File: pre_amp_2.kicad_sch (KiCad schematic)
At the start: 55 parts, among them J1 IN, J10 SW2_3, J11 SW2_1, J12 SW2_4, J13 VR5_3, J14 VR5_1, J15 OUT, J2 GND2, J3 Vin, J4 GND, J5 VR1_1, J6 VR3_3, J7 VR1_3, J9 VR4_2, SW1 bright, SW2 SW_SP3T, U1 TL072, U2 ICL7660

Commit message: 入力部分が抵抗(GND)->コンデンサ->ICだったのをコンデンサ->抵抗(GND)->ICに変更。 (直流がICにたまってGNDに落ちず音が出なくなる)
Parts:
- J6: value VR3_3 -> VR3_2
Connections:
- net at C1.1, J1.1 (Pin_1): no longer R1.2
- net at C1.2, U1.3 (+): now also R1.2
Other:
- moved on the sheet: C1, J2, R1
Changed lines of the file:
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@@
 	)
 	(junction
-		(at 39.37 91.44)
-		(diameter 0)
-		(color 0 0 0 0)
-	)
-	(junction
 		(at 205.74 151.13)
 		(diameter 0)
@@
 	)
 	(junction
-		(at 55.88 115.57)
-		(diameter 0)
-		(color 0 0 0 0)
-	)
-	(junction
 		(at 190.5 116.84)
 		(diameter 0)
@@
 	)
 	(junction
+		(at 55.88 116.84)
+		(diameter 0)
+		(color 0 0 0 0)
+	)
+	(junction
 		(at 111.76 19.05)
 		(diameter 0)
@@
 	)
 	(junction
+		(at 48.26 114.3)
+		(diameter 0)
+		(color 0 0 0 0)
+	)
+	(junction
 		(at 186.69 116.84)
 		(diameter 0)
@@
 	)
 	(junction
-		(at 212.09 116.84)
+		(at 48.26 91.44)
 		(diameter 0)
 		(color 0 0 0 0)
 	)
 	(junction
-		(at 167.64 116.84)
+		(at 212.09 116.84)
 		(diameter 0)
 		(color 0 0 0 0)
 	)
 	(junction
-		(at 140.97 19.05)
+		(at 167.64 116.84)
 		(diameter 0)
 		(color 0 0 0 0)
 	)
 	(junction
-		(at 39.37 113.03)
+		(at 140.97 19.05)
 		(diameter 0)
 		(color 0 0 0 0)
@@
 	(wire
 		(pts
+			(xy 34.29 91.44) (xy 39.37 91.44)
+		)
+		(stroke
+			(width 0)
+			(type default)
+		)
+	)
+	(wire
+		(pts
 			(xy 55.88 86.36) (xy 55.88 102.87)
 		)
@@
 	(wire
 		(pts
+			(xy 48.26 91.44) (xy 57.15 91.44)
+		)
+		(stroke
+			(width 0)
+			(type default)
+		)
+	)
+	(wire
+		(pts
 			(xy 111.76 19.05) (xy 125.73 19.05)
 		)
@@
 	(wire
 		(pts
+			(xy 55.88 116.84) (xy 55.88 118.11)
+		)
+		(stroke
+			(width 0)
+			(type default)
+		)
+	)
+	(wire
+		(pts
 			(xy 113.03 109.22) (xy 113.03 102.87)
 		)
@@
 	(wire
 		(pts
+			(xy 48.26 116.84) (xy 55.88 116.84)
+		)
+		(stroke
+			(width 0)
+			(type default)
+		)
+	)
+	(wire
+		(pts
 			(xy 219.71 105.41) (xy 231.14 105.41)
 		)
@@
 	(wire
 		(pts
-			(xy 39.37 113.03) (xy 39.37 115.57)
+			(xy 44.45 91.44) (xy 48.26 91.44)
 		)
 		(stroke
@@
 	(wire
 		(pts
-			(xy 39.37 91.44) (xy 44.45 91.44)
-		)
-		(stroke
-			(width 0)
-			(type default)
-		)
-	)
-	(wire
-		(pts
 			(xy 146.05 55.88) (xy 146.05 67.31)
 		)
@@
 	(wire
 		(pts
-			(xy 39.37 115.57) (xy 55.88 115.57)
+			(xy 190.5 113.03) (xy 195.58 113.03)
 		)
 		(stroke
@@
 	(wire
 		(pts
-			(xy 190.5 113.03) (xy 195.58 113.03)
+			(xy 48.26 104.14) (xy 48.26 91.44)
 		)
 		(stroke
@@
 	(wire
 		(pts
-			(xy 123.19 90.17) (xy 125.73 90.17)
+			(xy 48.26 109.22) (xy 48.26 114.3)
 		)
 		(stroke
@@
 	(wire
 		(pts
-			(xy 132.08 90.17) (xy 132.08 92.71)
+			(xy 123.19 90.17) (xy 125.73 90.17)
 		)
 		(stroke
@@
 	(wire
 		(pts
-			(xy 49.53 91.44) (xy 57.15 91.44)
+			(xy 132.08 90.17) (xy 132.08 92.71)
 		)
 		(stroke
@@
 	(wire
 		(pts
-			(xy 39.37 93.98) (xy 39.37 91.44)
-		)
-		(stroke
-			(width 0)
-			(type default)
-		)
-	)
-	(wire
-		(pts
 			(xy 180.34 151.13) (xy 184.15 151.13)
 		)
@@
 	(wire
 		(pts
-			(xy 39.37 99.06) (xy 39.37 113.03)
+			(xy 107.95 88.9) (xy 101.6 88.9)
 		)
 		(stroke
@@
 	(wire
 		(pts
-			(xy 107.95 88.9) (xy 101.6 88.9)
+			(xy 48.26 114.3) (xy 48.26 116.84)
 		)
 		(stroke
@@
 	(wire
 		(pts
-			(xy 55.88 115.57) (xy 55.88 118.11)
+			(xy 55.88 110.49) (xy 55.88 116.84)
 		)
 		(stroke
@@
 	(wire
 		(pts
-			(xy 55.88 115.57) (xy 55.88 110.49)
-		)
-		(stroke
-			(width 0)
-			(type default)
-		)
-	)
-	(wire
-		(pts
 			(xy 100.33 114.3) (xy 107.95 114.3)
 		)
@@
 	(wire
 		(pts
-			(xy 34.29 91.44) (xy 39.37 91.44)
-		)
-		(stroke
-			(width 0)
-			(type default)
-		)
-	)
-	(wire
-		(pts
 			(xy 196.85 134.62) (xy 196.85 138.43)
 		)
@@
 			)
 		)
-		(property "Value" "VR3_3"
+		(property "Value" "VR3_2"
 			(at 99.822 116.332 90)
 			(effects
@@
 	(symbol
 		(lib_id "Device:C_Small")
-		(at 46.99 91.44 90)
+		(at 41.91 91.44 90)
 		(unit 1)
 		(exclude_from_sim no)
@@
 		(dnp no)
 		(property "Reference" "C1"
-			(at 49.2125 87.9413 90)
+			(at 44.1325 87.9413 90)
 			(effects
 				(font
@@
 		)
 		(property "Value" "0.1u"
-			(at 49.2125 85.4075 90)
+			(at 44.1325 85.4075 90)
 			(effects
 				(font
@@
 		)
 		(property "Footprint" "MyLibrary:11.6_7.0_p7.5"
-			(at 46.99 91.44 0)
+			(at 41.91 91.44 0)
 			(effects
 				(font
@@
 		)
 		(property "Datasheet" "~"
-			(at 46.99 91.44 0)
+			(at 41.91 91.44 0)
 			(effects
 				(font
@@
 		)
 		(property "Description" "Unpolarized capacitor, small symbol"
-			(at 46.99 91.44 0)
+			(at 41.91 91.44 0)
 			(effects
 				(font
@@
 	(symbol
 		(lib_id "Device:R_Small")
-		(at 39.37 96.52 180)
+		(at 48.26 106.68 180)
 		(unit 1)
 		(exclude_from_sim no)
@@
 		(fields_autoplaced yes)
 		(property "Reference" "R1"
-			(at 41.91 95.2499 0)
+			(at 50.8 105.4099 0)
 			(effects
 				(font
@@
 		)
 		(property "Value" "1M"
-			(at 41.91 97.7899 0)
+			(at 50.8 107.9499 0)
 			(effects
 				(font
@@
 				)
 				(justify right)
+				(hide yes)
 			)
 		)
 		(property "Footprint" "Resistor_THT:R_Axial_DIN0204_L3.6mm_D1.6mm_P2.54mm_Vertical"
-			(at 39.37 96.52 0)
+			(at 48.26 106.68 0)
 			(effects
 				(font
@@
 		)
 		(property "Datasheet" "~"
-			(at 39.37 96.52 0)
+			(at 48.26 106.68 0)
 			(effects
 				(font
@@
 		)
 		(property "Description" "Resistor, small symbol"
-			(at 39.37 96.52 0)
+			(at 48.26 106.68 0)
 			(effects
 				(font
@@
 	(symbol
 		(lib_id "Connector:Conn_01x01_Pin")
-		(at 34.29 113.03 0)
+		(at 43.18 114.3 0)
 		(mirror x)
 		(unit 1)
@@
 		(dnp no)
 		(property "Reference" "J2"
-			(at 34.925 118.11 0)
+			(at 43.815 119.38 0)
 			(effects
 				(font
@@
 		)
 		(property "Value" "GND2"
-			(at 34.925 115.57 0)
+			(at 43.815 116.84 0)
 			(effects
 				(font
@@
 		)
 		(property "Footprint" "Connector_PinHeader_2.54mm:PinHeader_1x01_P2.54mm_Vertical"
-			(at 34.29 113.03 0)
+			(at 43.18 114.3 0)
 			(effects
 				(font
@@
 		)
 		(property "Datasheet" "~"
-			(at 34.29 113.03 0)
+			(at 43.18 114.3 0)
 			(effects
 				(font
@@
 		)
 		(property "Description" "Generic connector, single row, 01x01, script generated"
-			(at 34.29 113.03 0)
+			(at 43.18 114.3 0)
 			(effects
 				(font

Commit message: 基板からつなぐボリュームの先を変更
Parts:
- J5: value VR1_1 -> VR3_2
- J6: value VR3_2 -> VR3_3
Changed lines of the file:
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@@
 			)
 		)
-		(property "Value" "VR3_2"
+		(property "Value" "VR3_3"
 			(at 99.822 116.332 90)
 			(effects
@@
 			)
 		)
-		(property "Value" "VR1_1"
+		(property "Value" "VR3_2"
 			(at 101.346 94.488 90)
 			(effects

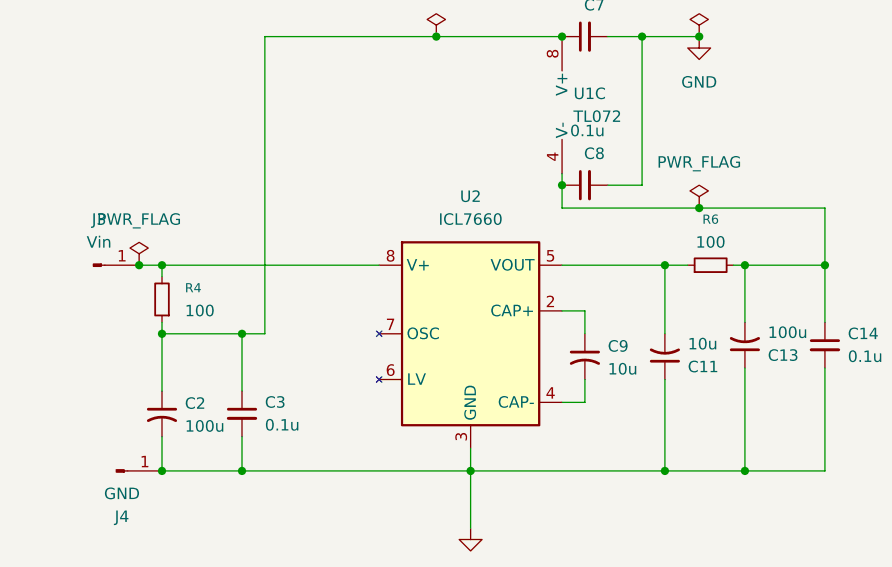
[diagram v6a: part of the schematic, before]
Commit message: TC1044Sに変更
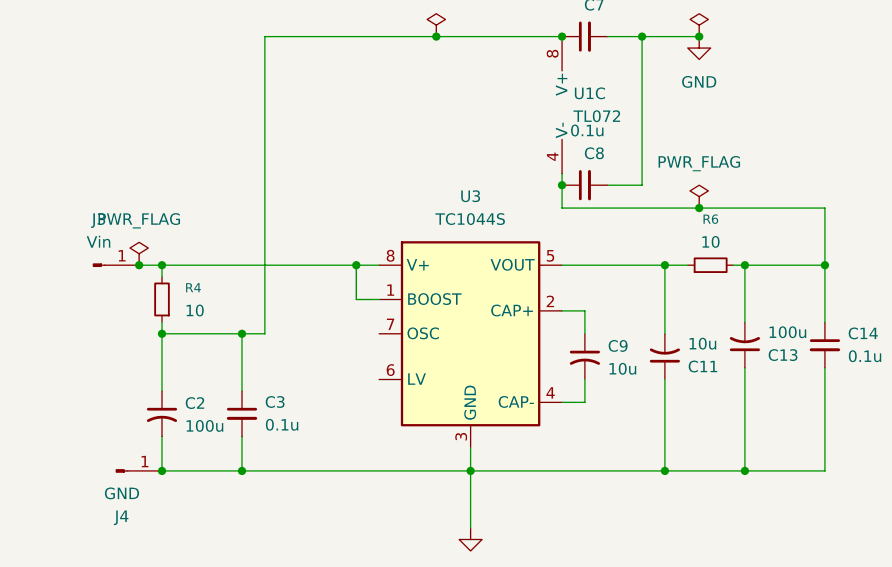
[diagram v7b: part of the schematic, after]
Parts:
- removed U2: ICL7660, Package_DIP:CERDIP-8_W7.62mm_SideBrazed_Socket, symbol Regulator_SwitchedCapacitor:ICL7660
- added U3: TC1044S, Package_DIP:CERDIP-8_W7.62mm_SideBrazed_Socket, symbol MyLibrary:TC1044S
- R4, R6: value 100 -> 10
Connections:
- net GND: now also U3.3 (GND)
- net at C9.1: now also U3.2 (CAP+)
- net at C9.2: now also U3.4 (CAP-)
- net at C11.2, R6.1: now also U3.5 (VOUT)
- net at J3.1 (Pin_1), R4.2: now also U3.1 (BOOST), U3.8 (V+)
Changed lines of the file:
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@@
 	)
 	(junction
+		(at 102.87 44.45)
+		(diameter 0)
+		(color 0 0 0 0)
+	)
+	(junction
 		(at 149.86 107.95)
 		(diameter 0)
@@
 	(wire
 		(pts
+			(xy 105.41 48.26) (xy 102.87 48.26)
+		)
+		(stroke
+			(width 0)
+			(type default)
+		)
+	)
+	(wire
+		(pts
 			(xy 90.17 52.07) (xy 90.17 58.42)
 		)
@@
 	(wire
 		(pts
+			(xy 102.87 44.45) (xy 105.41 44.45)
+		)
+		(stroke
+			(width 0)
+			(type default)
+		)
+	)
+	(wire
+		(pts
 			(xy 67.31 102.87) (xy 76.2 102.87)
 		)
@@
 	(wire
 		(pts
-			(xy 81.28 44.45) (xy 105.41 44.45)
+			(xy 81.28 44.45) (xy 102.87 44.45)
 		)
 		(stroke
@@
 	(wire
 		(pts
+			(xy 102.87 48.26) (xy 102.87 44.45)
+		)
+		(stroke
+			(width 0)
+			(type default)
+		)
+	)
+	(wire
+		(pts
 			(xy 123.19 95.25) (xy 123.19 104.14)
 		)
@@
 	)
 	(symbol
-		(lib_id "Regulator_SwitchedCapacitor:ICL7660")
-		(at 115.57 52.07 0)
-		(unit 1)
-		(exclude_from_sim no)
-		(in_bom yes)
-		(on_board yes)
-		(dnp no)
-		(fields_autoplaced yes)
-		(property "Reference" "U2"
-			(at 115.57 36.83 0)
-			(effects
-				(font
-					(size 1.27 1.27)
-				)
-			)
-		)
-		(property "Value" "ICL7660"
-			(at 115.57 39.37 0)
-			(effects
-				(font
-					(size 1.27 1.27)
-				)
-			)
-		)
-		(property "Footprint" "Package_DIP:CERDIP-8_W7.62mm_SideBrazed_Socket"
-			(at 118.11 54.61 0)
-			(effects
-				(font
-					(size 1.27 1.27)
-				)
-				(hide yes)
-			)
-		)
-		(property "Datasheet" "http://datasheets.maximintegrated.com/en/ds/ICL7660-MAX1044.pdf"
-			(at 118.11 54.61 0)
-			(effects
-				(font
-					(size 1.27 1.27)
-				)
-				(hide yes)
-			)
-		)
-		(property "Description" "Switched-Capacitor Voltage Converter, 1.5V to 10.0V operating supply voltage, 10mA with a 0.5V output drop, SO-8/DIP-8/µMAX-8/TO-99"
-			(at 115.57 52.07 0)
-			(effects
-				(font
-					(size 1.27 1.27)
-				)
-				(hide yes)
-			)
-		)
-		(pin "4"
-		)
-		(pin "1"
-		)
-		(pin "8"
-		)
-		(pin "3"
-		)
-		(pin "5"
-		)
-		(pin "2"
-		)
-		(pin "7"
-		)
-		(pin "6"
-		)
-		(instances
-			(project "pre_amp_2"
-				(path "/a24a43ce-b78c-4b02-8ea5-638bfbce1c81"
-					(reference "U2")
-					(unit 1)
-				)
-			)
-		)
-	)
-	(symbol
 		(lib_id "Device:R_Potentiometer")
 		(at 123.19 107.95 0)
@@
 	)
 	(symbol
+		(lib_id "MyLibrary:TC1044S")
+		(at 115.57 52.07 0)
+		(unit 1)
+		(exclude_from_sim no)
+		(in_bom yes)
+		(on_board yes)
+		(dnp no)
+		(fields_autoplaced yes)
+		(property "Reference" "U3"
+			(at 115.57 36.83 0)
+			(effects
+				(font
+					(size 1.27 1.27)
+				)
+			)
+		)
+		(property "Value" "TC1044S"
+			(at 115.57 39.37 0)
+			(effects
+				(font
+					(size 1.27 1.27)
+				)
+			)
+		)
+		(property "Footprint" "Package_DIP:CERDIP-8_W7.62mm_SideBrazed_Socket"
+			(at 118.11 54.61 0)
+			(effects
+				(font
+					(size 1.27 1.27)
+				)
+				(hide yes)
+			)
+		)
+		(property "Datasheet" "http://datasheets.maximintegrated.com/en/ds/ICL7660-MAX1044.pdf"
+			(at 118.11 54.61 0)
+			(effects
+				(font
+					(size 1.27 1.27)
+				)
+				(hide yes)
+			)
+		)
+		(property "Description" "Switched-Capacitor Voltage Converter, 1.5V to 10.0V operating supply voltage, 10mA with a 0.5V output drop, SO-8/DIP-8/µMAX-8/TO-99"
+			(at 115.57 52.07 0)
+			(effects
+				(font
+					(size 1.27 1.27)
+				)
+				(hide yes)
+			)
+		)
+		(pin "8"
+		)
+		(pin "7"
+		)
+		(pin "5"
+		)
+		(pin "4"
+		)
+		(pin "2"
+		)
+		(pin "1"
+		)
+		(pin "6"
+		)
+		(pin "3"
+		)
+		(instances
+			(project ""
+				(path "/a24a43ce-b78c-4b02-8ea5-638bfbce1c81"
+					(reference "U3")
+					(unit 1)
+				)
+			)
+		)
+	)
+	(symbol
 		(lib_id "power:GND")
 		(at 140.97 19.05 0)
@@
 			)
 		)
-		(property "Value" "100"
+		(property "Value" "10"
 			(at 83.82 49.5299 0)
 			(effects
@@
 			)
 		)
-		(property "Value" "100"
+		(property "Value" "10"
 			(at 142.24 41.91 90)
 			(effects
